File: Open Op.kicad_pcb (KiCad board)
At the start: 2 copper layers, 86.4 x 110 mm, 143 parts, among them J1 Conn_01x02_Female, J2 AudioJack3_Ground, J3 Conn_01x04_Male, Q1 BSS138, Q2 BSS138, SW1 Rotary_Encoder_Switch, SW2 Rotary_Encoder_Switch, SW3 Rotary_Encoder_Switch, SW4 Rotary_Encoder_Switch, SW5 SW_Push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

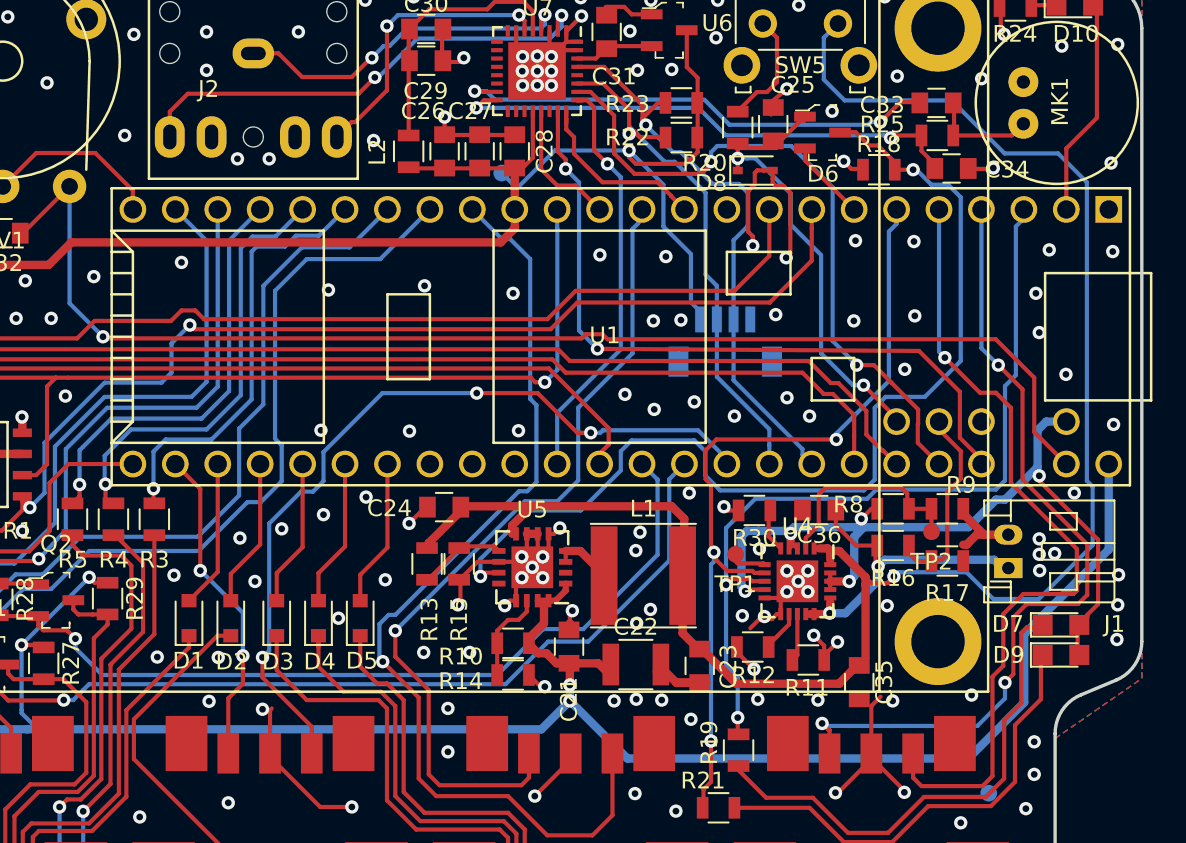
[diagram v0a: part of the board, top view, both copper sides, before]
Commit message: trying pins 0 and 1 for apa102
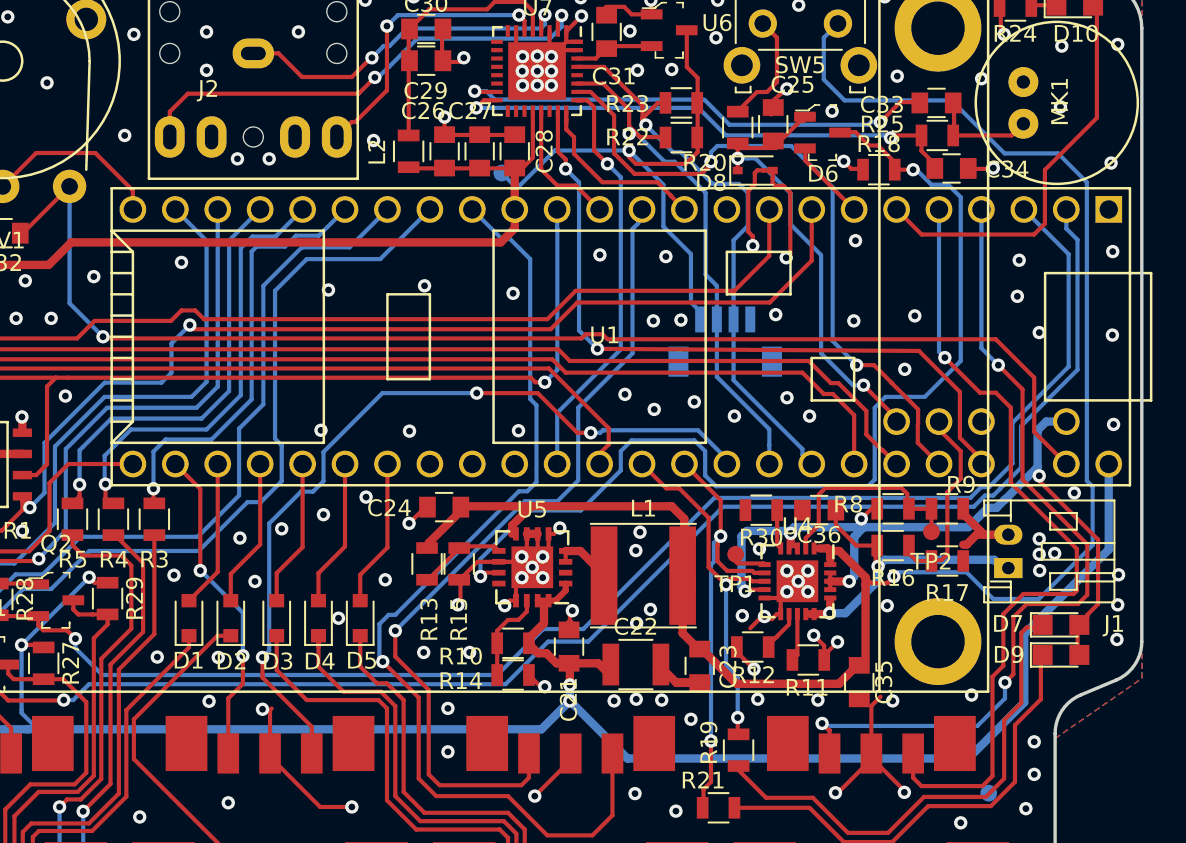
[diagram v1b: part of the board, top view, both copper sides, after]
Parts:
- moved R30 0.41 mm to (120.4, 69.1)
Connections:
- U1 pad 2: REC_LED -> RGB_CLOCK
- U1 pad 3: BATT_STAT1 -> RGB_DATA
- U1 pad 42: RGB_DATA -> BATT_STAT1
- U1 pad 43: RGB_CLOCK -> BATT_STAT2
- U1 pad 6: BATT_STAT2 -> REC_LED
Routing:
- net RGB_DATA: track 50.5 -> 85.8 mm
- net RGB_CLOCK: track 53.7 -> 88.1 mm
- net BATT_STAT1: track 49.4 -> 21.4 mm
- net BATT_STAT2: track 49.2 -> 26.6 mm, vias 3 -> 2
- net REC_LED: track 13.0 -> 24.1 mm
- net GND: track 154.8 -> 153.9 mm, vias 276 -> 274

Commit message: ordered 0.9.0
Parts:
- moved REF*** 47.4 mm to (116.1, 141.1)
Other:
- board text added: "(C) 2018 Chris Miller"
- board text added: "Teensy Beats Shield 0.9.0"
